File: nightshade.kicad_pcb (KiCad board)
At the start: 4 copper layers, 153.3 x 70.8 mm, 81 parts, among them J1 Bus_ISA_16bit, J2 DE15_Plug_HighDensity_Mountin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, U1 GD542x_ISA, U2 SOJ_256Kx16, U3 SOJ_256Kx16, U4 LM334M, U5 LDK320AM50R, U6 27C256, U7 74LS244, Y1 14.31818MHz

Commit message: Add files via upload
Updated with corrected parts lists etc.
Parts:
- C1, C10, C2, C3, C4, C5, C6, C9: value 0.1u -> 0.22u
- C11, C12: value 27p -> 18p
- C22, C24, C25: value 18pF -> 12p
- C26, C28, C29: value 10pF -> 12p
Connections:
- U4 pad 5: (no net) -> unconnected-(U4-NC-Pad5)
- U4 pad 8: (no net) -> unconnected-(U4-NC-Pad8)
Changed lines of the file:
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@@
 	(net 209 "Net-(U6-D4)")
 	(net 210 "Net-(U6-D6)")
+	(net 211 "unconnected-(U4-NC-Pad8)")
+	(net 212 "unconnected-(U4-NC-Pad5)")
 	(footprint "Capacitor_SMD:C_1206_3216Metric"
 		(layer "F.Cu")
@@
 			)
 		)
-		(property "Value" "0.1u"
+		(property "Value" "0.22u"
 			(at -0.01 -2.35 90)
 			(layer "F.Fab")
@@
 			)
 		)
-		(property "Value" "0.1u"
+		(property "Value" "0.22u"
 			(at -1.525 1.425 90)
 			(layer "F.Fab")
@@
 			)
 		)
-		(property "Value" "27p"
+		(property "Value" "18p"
 			(at 0 1.68 90)
 			(layer "F.Fab")
@@
 			)
 		)
-		(property "Value" "27p"
+		(property "Value" "18p"
 			(at 0 1.68 90)
 			(layer "F.Fab")
@@
 			)
 		)
-		(property "Value" "18pF"
+		(property "Value" "12p"
 			(at 0 1.68 90)
 			(layer "F.Fab")
@@
 			)
 		)
-		(property "Value" "18pF"
+		(property "Value" "12p"
 			(at 0 1.68 90)
 			(layer "F.Fab")
@@
 			)
 		)
-		(property "Value" "18pF"
+		(property "Value" "12p"
 			(at 0 1.68 90)
 			(layer "F.Fab")
@@
 			)
 		)
-		(property "Value" "10pF"
+		(property "Value" "12p"
 			(at 0 1.68 90)
 			(layer "F.Fab")
@@
 			)
 		)
-		(property "Value" "10pF"
+		(property "Value" "12p"
 			(at 0 1.68 90)
 			(layer "F.Fab")
@@
 			)
 		)
-		(property "Value" "10pF"
+		(property "Value" "12p"
 			(at 0 1.68 90)
 			(layer "F.Fab")
@@
 			(layers "F.Cu" "F.Paste" "F.Mask")
 			(roundrect_rratio 0.25)
+			(net 212 "unconnected-(U4-NC-Pad5)")
+			(pinfunction "NC")
+			(pintype "no_connect")
 		)
 		(pad "6" smd roundrect
@@
 			(layers "F.Cu" "F.Paste" "F.Mask")
 			(roundrect_rratio 0.25)
+			(net 211 "unconnected-(U4-NC-Pad8)")
+			(pinfunction "NC")
+			(pintype "no_connect")
 		)
 		(model "${KICAD8_3DMODEL_DIR}/Package_SO.3dshapes/SOIC-8_3.9x4.9mm_P1.27mm.step"
@@
 			)
 		)
-		(property "Value" "0.1u"
+		(property "Value" "0.22u"
 			(at 1.35 1.45 0)
 			(layer "B.Fab")
@@
 			)
 		)
-		(property "Value" "0.1u"
+		(property "Value" "0.22u"
 			(at -3.625 0.025 0)
 			(layer "B.Fab")
@@
 			)
 		)
-		(property "Value" "0.1u"
+		(property "Value" "0.22u"
 			(at -2.575 -1.65 90)
 			(layer "B.Fab")
@@
 			)
 		)
-		(property "Value" "0.1u"
+		(property "Value" "0.22u"
 			(at 2.55 -1.1 0)
 			(layer "B.Fab")
@@
 			)
 		)
-		(property "Value" "0.1u"
+		(property "Value" "0.22u"
 			(at 0 -1.68 0)
 			(layer "B.Fab")
@@
 			)
 		)
-		(property "Value" "0.1u"
+		(property "Value" "0.22u"
 			(at -3.675 0.025 0)
 			(layer "B.Fab")

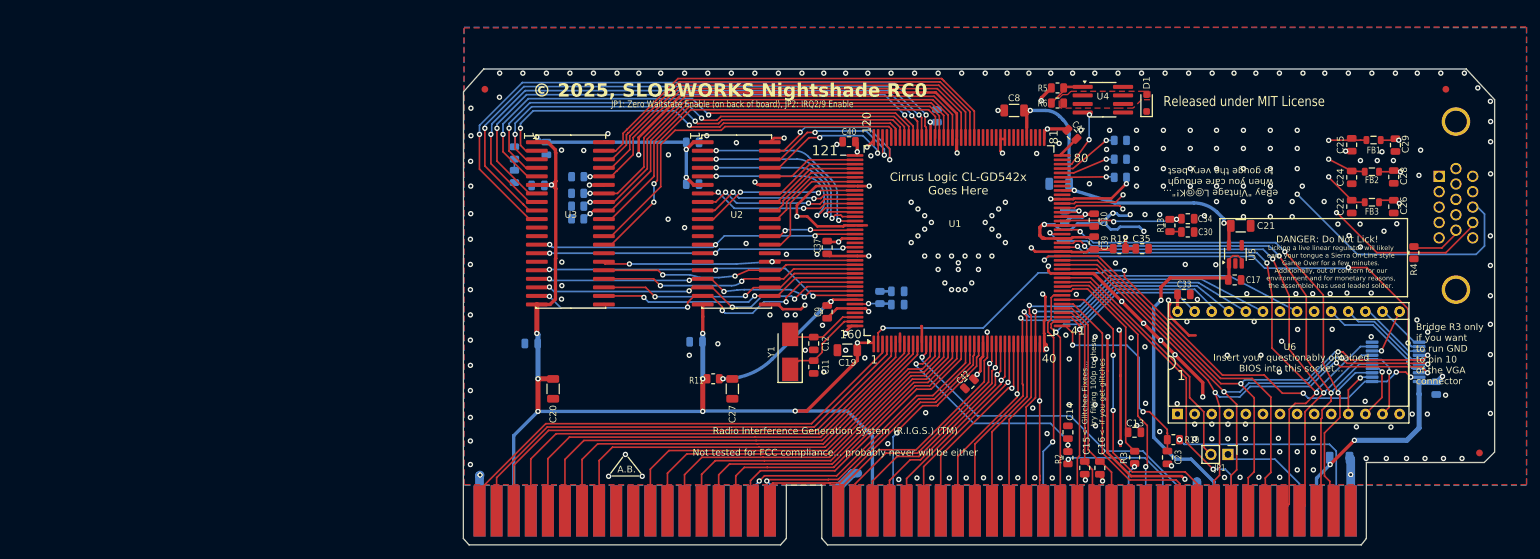
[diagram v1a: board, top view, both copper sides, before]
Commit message: Add files via upload
Updated to KiCAD 9.x, fixed some bugs in the silkscreening
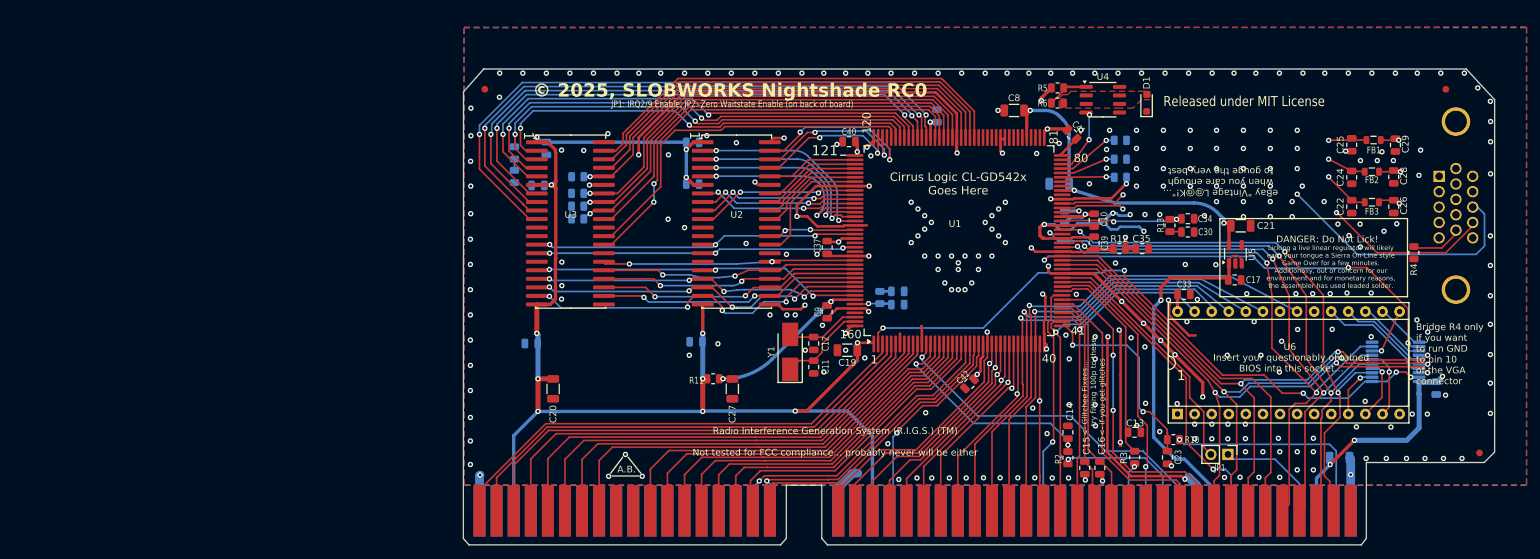
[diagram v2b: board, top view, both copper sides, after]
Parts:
- U4: footprint PDVGA:SOIC-8_DMP-8 -> Package_SO:SOIC-8_3.9x4.9mm_P1.27mm
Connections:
- U4 pad 5: unconnected-(U4-NC-Pad5) -> (no net)
- U4 pad 8: unconnected-(U4-NC-Pad8) -> (no net)
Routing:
- net GND: track 309.2 -> 310.4 mm
- net /+12V: track 55.6 -> 55.0 mm
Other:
- board text added: "Bridge R4 only if you want to run GND to pin 10 of the VGA connector"
- board text added: "JP1: IRQ2/9 Enable, JP2: Zero Waitstate Enable (on back of board)"
- board text removed: "Bridge R3 only if you want to run GND to pin 10 of the VGA connector"
- board text removed: "JP1: Zero Waitstate Enable (on back of board), JP2: IRQ2/9 Enable"

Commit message: Add files via upload
Updated to Cherry Tomato V1.0 revision
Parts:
- removed C21: 10u, Capacitor_SMD:C_1206_3216Metric
- removed C3, C6: 0.22u, Capacitor_SMD:C_0805_2012Metric
- removed D1: 1N4148WS, Diode_SMD:D_SOD-323_HandSoldering
- removed FB1, FB2, FB3: 0805, Inductor_SMD:L_0805_2012Metric
- removed the G*** at (127.9, 117.0)
- removed U7: 74LS244, Package_SO:SSOP-20_5.3x7.2mm_P0.65mm
- added C43: 10u, Capacitor_SMD:C_1206_3216Metric, F.Cu at (145.6, 144.4)
- added F1: 0805L020YR, Fuse:Fuse_0805_2012Metric, B.Cu at (228.5, 115.1)
- added G***: LOGO, SOJ_DRAM:tomato2, F.Cu at (169.5, 139.8)
- added J3: Conn_02x13_Odd_Even, Connector_PinHeader_2.54mm:PinHeader_2x13_P2.54mm_Vertical, F.Cu at (186.2, 85.2)
- added JP3: 16bit_BIOS, Connector_PinHeader_2.54mm:PinHeader_1x02_P2.54mm_Vertical, F.Cu at (84.8, 112.2)
- added L1: 1210, Inductor_SMD:L_1206_3216Metric, F.Cu at (214.7, 94.5)
- added L2: 1210, Inductor_SMD:L_1206_3216Metric, F.Cu at (214.7, 97.9)
- added L3: 1210, Inductor_SMD:L_1206_3216Metric, F.Cu at (214.7, 101.3)
- added Q1: MMBT3904, Package_TO_SOT_SMD:SOT-23, B.Cu at (173.5, 99.4)
- added R20: 33, Resistor_SMD:R_0603_1608Metric, B.Cu at (163.2, 108.1)
- added R21: 6.8K, Resistor_SMD:R_0805_2012Metric, F.Cu at (84.8, 118.2)
- added R22: 33, Resistor_SMD:R_0805_2012Metric, F.Cu at (184.7, 143.7)
- added R23: 1K, Resistor_SMD:R_0603_1608Metric, F.Cu at (158.9, 91.4)
- added R24: 1K, Resistor_SMD:R_0603_1608Metric, F.Cu at (157.1, 91.4)
- added R25: 16, Resistor_SMD:R_0603_1608Metric, B.Cu at (183.7, 104.0)
- added R26: 16, Resistor_SMD:R_0603_1608Metric, B.Cu at (183.7, 106.0)
- added U10: 74HCT244, PDVGA:SSOP-20_4.4_5.3x6.5mm_P0.65mm, F.Cu at (105.0, 141.8)
- added U12: L78L05_TO92, Package_TO_SOT_THT:TO-92_Inline, F.Cu at (201.0, 105.1)
- added U8: 74HCT244, PDVGA:SSOP-20_4.4_5.3x6.5mm_P0.65mm, F.Cu at (181.7, 122.5)
- added U9: 27C256, Package_DIP:DIP-28_W15.24mm_Socket, F.Cu at (188.2, 143.8)
- C1, C2, C32, C36, C38, C4, C5: value 0.22u -> 0.1u; moved to F.Cu
- C10, C17, C34, C35, C37, C39, C40, C41, C42, C9: value 0.22u -> 0.1u
- C15: value 100p -> 10u; footprint Capacitor_SMD:C_0805_2012Metric -> Capacitor_SMD:C_1206_3216Metric
- C16: value 100p -> 4.7u; footprint Capacitor_SMD:C_0805_2012Metric -> Capacitor_SMD:CP_Elec_3x5.4
- C18, C31, R14, R15, R16, R17, R18, R19: moved to F.Cu
- C22: value 12p -> 0.1u
- C24, C25: value 12p -> 0.1u; moved to B.Cu
- C26, C28, C29: value 12p -> 47pF; footprint Capacitor_SMD:C_0805_2012Metric -> Capacitor_SMD:C_0603_1608Metric
- C33: value 0.22u -> 0.1u; moved to B.Cu
- C7, C8: value 2.2u -> 10u
- JP2: footprint Resistor_SMD:R_0805_2012Metric -> Connector_PinHeader_2.54mm:PinHeader_1x02_P2.54mm_Vertical; moved to F.Cu
- R11, R12: footprint Resistor_SMD:R_0805_2012Metric -> Resistor_SMD:R_0603_1608Metric
- R2: value 47 -> 33; footprint Resistor_SMD:R_0805_2012Metric -> Resistor_SMD:R_0603_1608Metric
- R4: value EhWot -> 33; footprint Resistor_SMD:R_0805_2012Metric -> Resistor_SMD:R_0603_1608Metric; moved to B.Cu
- R5: value 150 -> 1K; moved to B.Cu
- R6: value 15 -> 270-300; moved to B.Cu
- R7, R8, R9: footprint Resistor_SMD:R_0805_2012Metric -> Resistor_SMD:R_0603_1608Metric; moved to F.Cu
- U4: value LM334M -> TL431DBZ; footprint Package_SO:SOIC-8_3.9x4.9mm_P1.27mm -> Package_TO_SOT_SMD:SOT-23; moved to B.Cu
- U5: value LDK320AM50R -> 93CxxA; footprint Package_TO_SOT_SMD:SOT-23-5_HandSoldering -> PDVGA:SOIC-8_DMP-8; moved to B.Cu
- moved C22 106.2 mm to (111.9, 140.1)
- moved FID1 89.9 mm to (137.2, 94.8)
- moved R4 59.6 mm to (163.2, 106.6), turned to 180 degrees
- moved C15 57.6 mm to (230.5, 139.8), turned to 180 degrees
- moved C24 56.4 mm to (157.2, 111.3), turned to 180 degrees
- moved R2 54.5 mm to (160.7, 91.4)
- moved C32 51.9 mm to (176.8, 117.0), turned to -90 degrees
- moved C16 46.1 mm to (197.0, 105.8), turned to -90 degrees
- moved C25 39.5 mm to (185.7, 127.0), turned to -90 degrees
- moved U5 38.7 mm to (158.2, 105.0), turned to -90 degrees
- moved C5 23.7 mm to (113.7, 128.0), turned to 90 degrees
- moved C31 20.6 mm to (126.4, 127.9), turned to -90 degrees
- moved JP1 19.9 mm to (179.2, 131.9), turned to 180 degrees
- moved C17 17.0 mm to (207.0, 106.0), turned to -90 degrees
- moved C18 15.0 mm to (225.3, 139.8)
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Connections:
- net /~{MEMW} renamed /~{SMEMW}
- C15 pad 1: GND -> /+12V
- C15 pad 2: /SA15 -> GND
- C16 pad 1: GND -> /AVcc
- C16 pad 2: /SA16 -> GND
- C22 pad 2: /BLUE -> /+5V
- C24 pad 2: /GREEN -> /+5V
- C25 pad 2: /RED -> /+5V
- J1 pad 12: Net-(J1-~{SMEMR}) -> /~{SMEMR}
- J2 pad 10: Net-(J2-Pad10) -> GND
- J2 pad 13: /HSYNC -> /VHSYNC
- J2 pad 14: /VSYNC -> /VVSYNC
- J2 pad 9: unconnected-(J2-Pad9) -> Net-(F1-Pad2)
- R1 pad 2: /VCLKVCC -> /+5V
- R2 pad 1: Net-(J1-~{SMEMR}) -> /DCLK
- R2 pad 2: /~{MEMR} -> Net-(J3-Pin_18)
- R4 pad 1: Net-(J2-Pad10) -> /HSYNC
- R4 pad 2: GND -> /FHSYNC
- R5 pad 1: GND -> /AVcc
- R5 pad 2: Net-(R5-Pad2) -> Net-(Q1-B)
- R6 pad 1: Net-(R5-Pad2) -> Net-(Q1-E)
- R6 pad 2: Net-(D1-A) -> GND
- U1 pad 73: unconnected-(U1-EEDI-Pad73) -> /EEDI
- U1 pad 74: unconnected-(U1-EECS-Pad74) -> /EECS
- U4 pad 1: Net-(R5-Pad2) -> Net-(Q1-B)
- U4 pad 2: Net-(D1-A) -> Net-(Q1-E)
- U4 pad 3: Net-(D1-A) -> GND
- U5 pad 1: /+12V -> /EECS
- U5 pad 2: GND -> /ESYNC
- U5 pad 3: /+12V -> /EVIDEO
- U5 pad 4: unconnected-(U5-BP-Pad4) -> /EEDI
- U5 pad 5: /AVcc -> GND
- U6 pad 1: unconnected-(U6-VPP-Pad1) -> /+5V
- U6 pad 11: Net-(U6-D0) -> /D0
- U6 pad 12: Net-(U6-D1) -> /D1
- U6 pad 13: Net-(U6-D2) -> /D2
- U6 pad 15: Net-(U6-D3) -> /D3
- U6 pad 16: Net-(U6-D4) -> /D4
- U6 pad 17: Net-(U6-D5) -> /D5
- U6 pad 18: Net-(U6-D6) -> /D6
- U6 pad 19: Net-(U6-D7) -> /D7
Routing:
- net /+5V: track 457.5 -> 207.3 mm, vias 21 -> 20
- net /D11: track 0.00 -> 132.1 mm, vias 0 -> 1
- net /D10: track 0.00 -> 129.2 mm, vias 0 -> 1
- net /D9: track 0.00 -> 124.5 mm, vias 0 -> 1
- net /D8: track 0.00 -> 122.4 mm, vias 0 -> 1
- net /D12: track 0.00 -> 115.5 mm, vias 0 -> 1
- net /D13: track 0.00 -> 112.5 mm, vias 0 -> 1
- net /D14: track 0.00 -> 109.5 mm, vias 0 -> 1
- net /D15: track 0.00 -> 108.0 mm, vias 0 -> 1
- net /SD3: track 124.3 -> 54.5 mm, vias 3 -> 0
- net GND: track 310.4 -> 242.6 mm, vias 310 -> 204
- net /VVSYNC: track 0.00 -> 62.1 mm, vias 0 -> 1
- net /VHSYNC: track 0.00 -> 56.2 mm
- net /+12V: track 55.0 -> 109.3 mm, vias 1 -> 4
- net /HSYNC: track 74.7 -> 20.5 mm
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- added copper zone on In2.Cu, net /+5V
- removed copper zone on F.Cu, net Net-(D1-A)
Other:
- board size 153.3 x 70.8 mm -> 153.4 x 76.2 mm
- board text added: "(C) 2026 SLOBWORKS"
- board text added: "(Optional)"
- board text added: "10uF"
- board text added: "27C256"
- board text added: "3904"
- board text added: "74HCT244"
- board text added: "78L05"
- board text added: "93C46"
- board text added: "C32"
- board text added: "CHERRY TOMATO V1.1"
- board text added: "DAC_AVcc"
- board text added: "DISGUSTINGLY USELESS -> VESA FEATURE CONNECTOR"
- board text added: "Designed by AB in California Released under MIT License"
- board text added: "HIGH BYTE"
- board text added: "LOW BYTE"
- board text added: "Memory Speed Table ~{R18 open,R19 open=37.5MHz} R18 open,R19 6.8K= 41.2MHz R18 6.8K, R19 open=44.7MHz R18 6.8K, R19 6.8K= 50.0MHz"
- board text added: "Nightshade"
- board text added: "Put yer ugly little GD542x here >:)"
- board text added: "Radio Interference Generation System (R.I.G.S.)(tm) Not tested for FCC compliance... probably never will be either"
- board text added: "THE 16-BIT STRAW OF PURE CHOKEHOLD"
- board text added: "TL431"
- board text added: "U6"
- board text added: "User Jumper Table ~{JP1: IRQ2/9 Enable} JP2: Zero Waitstate Enable JP3: 16-Bit BIOS Enable (on=16-bit)"
- board text added: "a27004a714f54ecec9eed07aae3e28bf"
- board text removed: "<- Glitchee Fixees... try fitting 100p to these, <- if you get glitches"
- board text removed: "A.B."
- board text removed: "Bridge R4 only if you want to run GND to pin 10 of the VGA connector"
- board text removed: "Cirrus Logic CL-GD542x Goes Here"
- board text removed: "DANGER: Do Not Lick!"
- board text removed: "Designed by AB in California"
- board text removed: "Insert your questionably obtained BIOS into this socket..."
- board text removed: "JP1: IRQ2/9 Enable, JP2: Zero Waitstate Enable (on back of board)"
- board text removed: "Licking a live linear regulator will likely earn your tongue a Sierra On-Line style Game Over for a few minutes. Additionally, out of concern for our environment and for monetary reasons, the assembler has used leaded solder."
- board text removed: "Memory Speed Table ------------- R18 open,R19 open=37.5MHz R18 open,R19 6.8K= 41.2MHz R18 6.8K, R19 open=44.7MHz R18 6.8K, R19 6.8K= 50.0MHz"
- board text removed: "Radio Interference Generation System (R.I.G.S.) (TM) Not tested for FCC compliance... probably never will be either"
- board text removed: "Released under MIT License"
- board text removed: "Unfortunately, circuit boards don't taste good. Do not ask me how I know"
- board text removed: "Who needs good"
- board text removed: "blue,"
- board text removed: "eBay "Vintage L@@K!"... when you care enough to gouge the very best"
- board text removed: "electrical layout"
- board text removed: "people?"
- board text removed: "puppy-dog"
- board text removed: "three-fingered"
- board text removed: "when we have"
- board text removed: "© 2025, SLOBWORKS Nightshade RC0"
